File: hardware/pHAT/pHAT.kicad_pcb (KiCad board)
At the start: 2 copper layers, 65 x 30 mm, 5 parts, among them P1 Conn_02x20_Odd_Even

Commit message: First version of PCB for pHAT
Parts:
- added C0: 0.1µ, Capacitor_SMD:C_0805_2012Metric_Pad1.15x1.40mm_HandSolder, F.Cu at (224.1, 131.3)
- added C1: 4.7µ, Capacitor_SMD:C_0805_2012Metric_Pad1.15x1.40mm_HandSolder, F.Cu at (221.6, 131.3)
- added J_Air: Conn_01x04, Connector_Molex:Molex_KK-254_AE-6410-04A_1x04_P2.54mm_Vertical, F.Cu at (229.2, 146.8)
- added J_Hive: Conn_01x04, Connector_Molex:Molex_KK-254_AE-6410-04A_1x04_P2.54mm_Vertical, F.Cu at (241.3, 146.8)
- added J_Weight: Conn_01x02, Connector_Molex:Molex_KK-254_AE-6410-02A_1x02_P2.54mm_Vertical, F.Cu at (253.3, 146.8)
- added R0: 5K, Resistor_SMD:R_0805_2012Metric_Pad1.15x1.40mm_HandSolder, F.Cu at (218.4, 129.0)
- added R1: 5K, Resistor_SMD:R_0805_2012Metric_Pad1.15x1.40mm_HandSolder, F.Cu at (234.3, 131.3)
- added R2: 5K, Resistor_SMD:R_0805_2012Metric_Pad1.15x1.40mm_HandSolder, F.Cu at (231.8, 131.3)
- added R3: 5K, Resistor_SMD:R_0805_2012Metric_Pad1.15x1.40mm_HandSolder, F.Cu at (233.7, 138.5)
- added R4: 5K, Resistor_SMD:R_0805_2012Metric_Pad1.15x1.40mm_HandSolder, F.Cu at (237.5, 138.5)
- added R5: 5K, Resistor_SMD:R_0805_2012Metric_Pad1.15x1.40mm_HandSolder, F.Cu at (236.8, 131.3)
- added R6: 5K, Resistor_SMD:R_0805_2012Metric_Pad1.15x1.40mm_HandSolder, F.Cu at (239.4, 131.3)
- added R7: 5K, Resistor_SMD:R_0805_2012Metric_Pad1.15x1.40mm_HandSolder, F.Cu at (229.2, 131.3)
- added R8: 5K, Resistor_SMD:R_0805_2012Metric_Pad1.15x1.40mm_HandSolder, F.Cu at (226.7, 131.3)
- added U0: PCA9540B, Package_SO:TSSOP-8_3x3mm_P0.65mm, F.Cu at (235.6, 135.4)
- added U1: ADC101C021CIMK, Package_TO_SOT_SMD:SOT-23-6, F.Cu at (218.4, 131.6)
- moved MK1 26.0 mm to (203.5, 123.5)
- moved MK2 26.0 mm to (261.5, 123.5)
- moved MK3 26.0 mm to (203.5, 146.5)
- moved MK4 26.0 mm to (261.5, 146.5)
- moved P1 26.0 mm to (208.4, 124.8)
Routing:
- net +3V3: track 0.00 -> 132.2 mm
- net /AnalogIn: track 0.00 -> 54.0 mm
- net /SDA: track 0.00 -> 34.9 mm
- net /SCL: track 0.00 -> 33.2 mm
- net /SCL1: track 0.00 -> 25.7 mm
- net /SDA1: track 0.00 -> 24.9 mm
- net GND: track 0.00 -> 20.2 mm, vias 0 -> 1
- net /SCL0: track 0.00 -> 17.8 mm
- net /SDA0: track 0.00 -> 16.4 mm
- net Net-(R0-Pad1): track 0.00 -> 3.06 mm
- net Net-(R7-Pad2): track 0.00 -> 2.54 mm
- added copper zone on B.Cu, net GND
- added copper zone on F.Cu, net GND

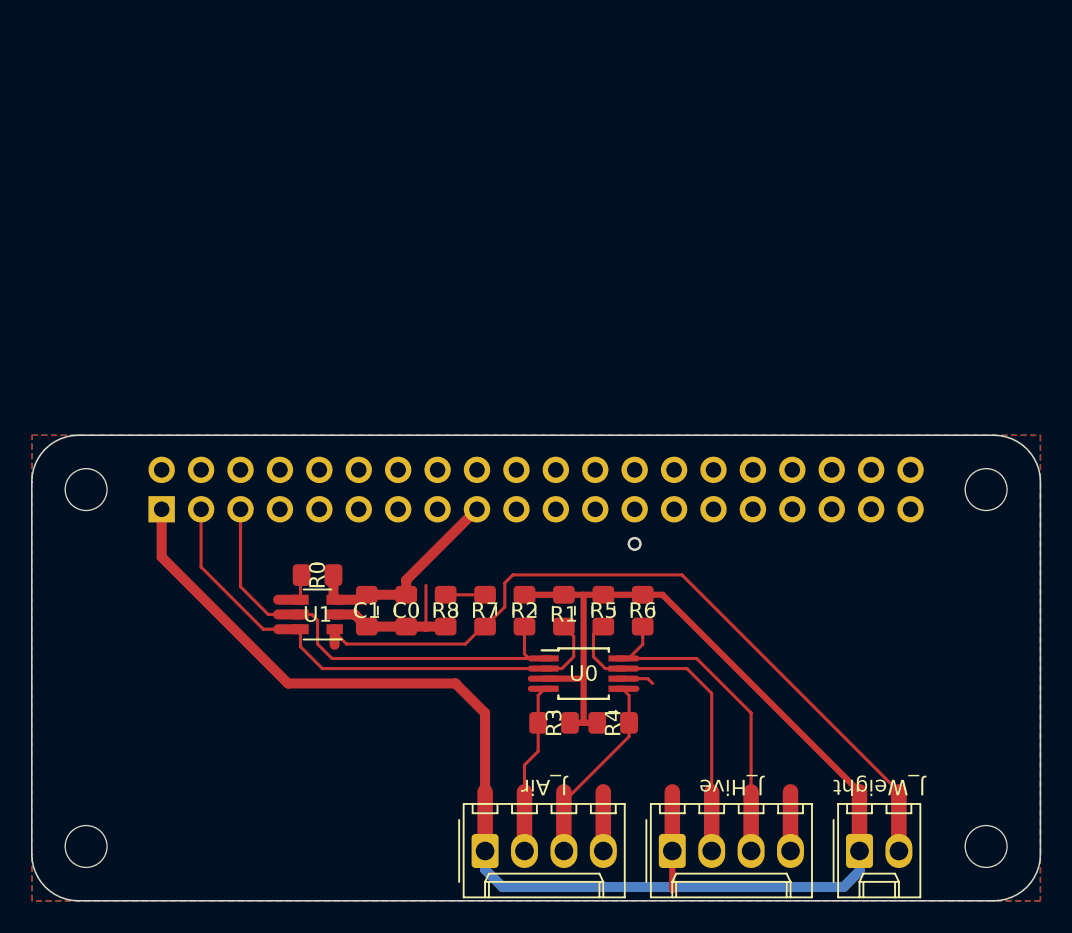
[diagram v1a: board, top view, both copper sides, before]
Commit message: graphical improvements to PCB
Added a logo and cleaned some tracks
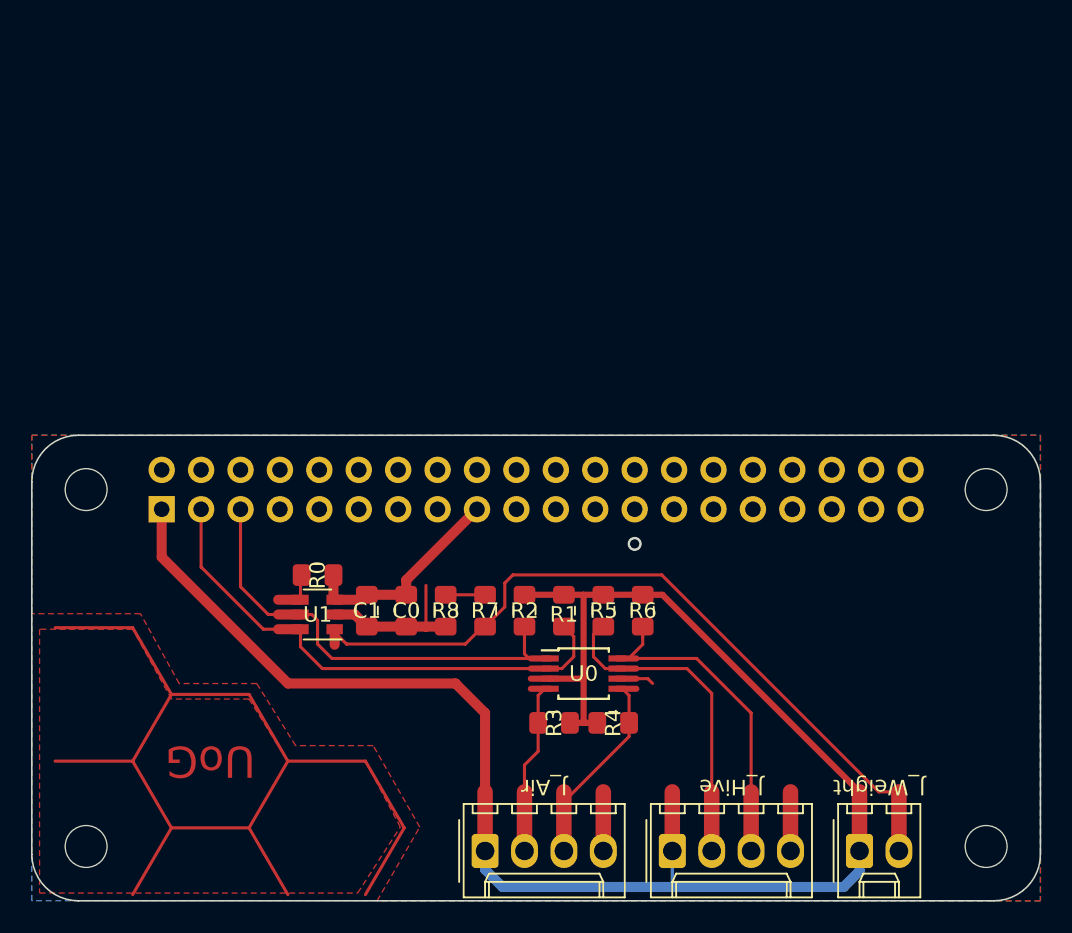
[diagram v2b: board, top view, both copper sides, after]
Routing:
- net Net-(P1-Pad10): track 0.00 -> 69.8 mm
- net +3V3: track 132.2 -> 129.7 mm
- added copper zone on F.Cu, net (none)
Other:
- rule trace_min: 0.1524 -> 0.2
- board text added: "UoG"

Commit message: First version of sensor board
Added a sensor board for the HIH61 humidity and temperature sensor
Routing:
- net Net-(P1-Pad10): track 69.8 -> 0.00 mm
- net +3V3: track 129.7 -> 199.4 mm

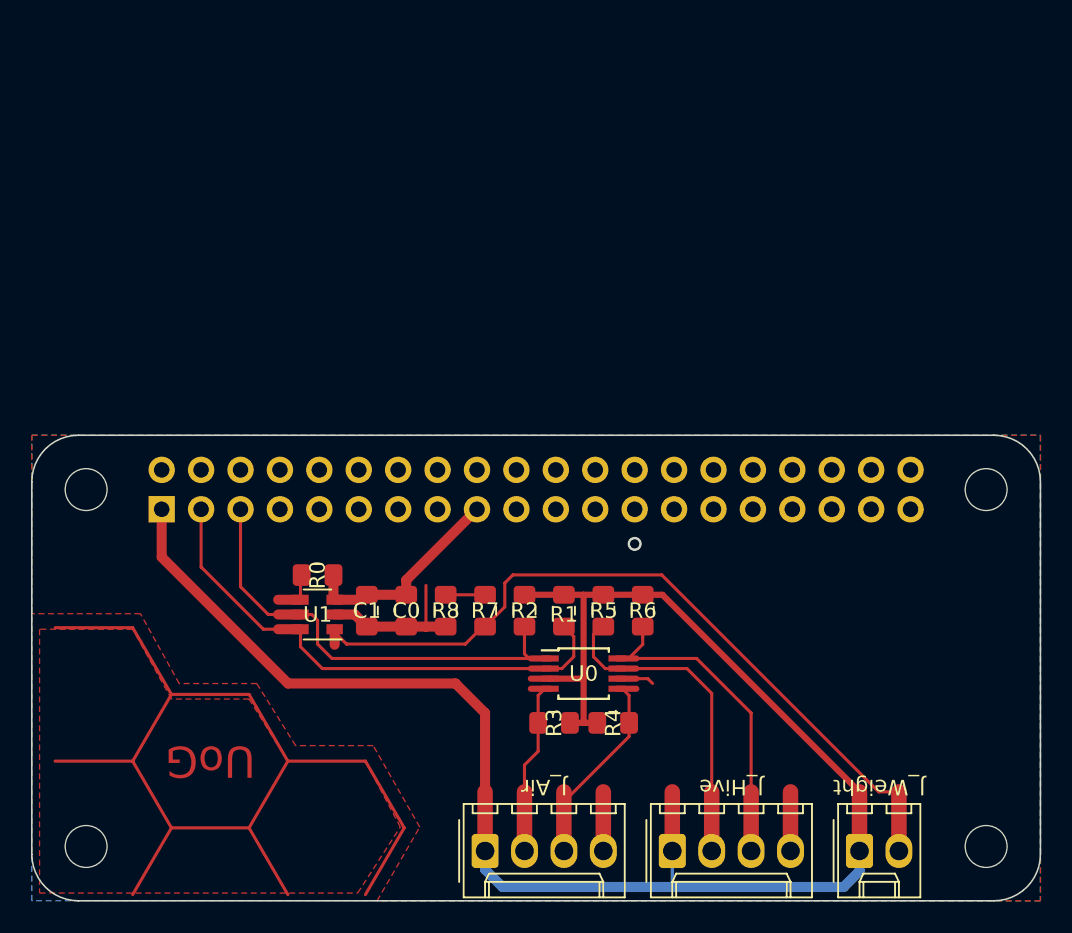
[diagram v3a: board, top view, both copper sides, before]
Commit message: Moving form multiplexer to two I2C busses
Changed from using one I2C bus with a multiplexer to using two I2C busses with the addition of level shifters
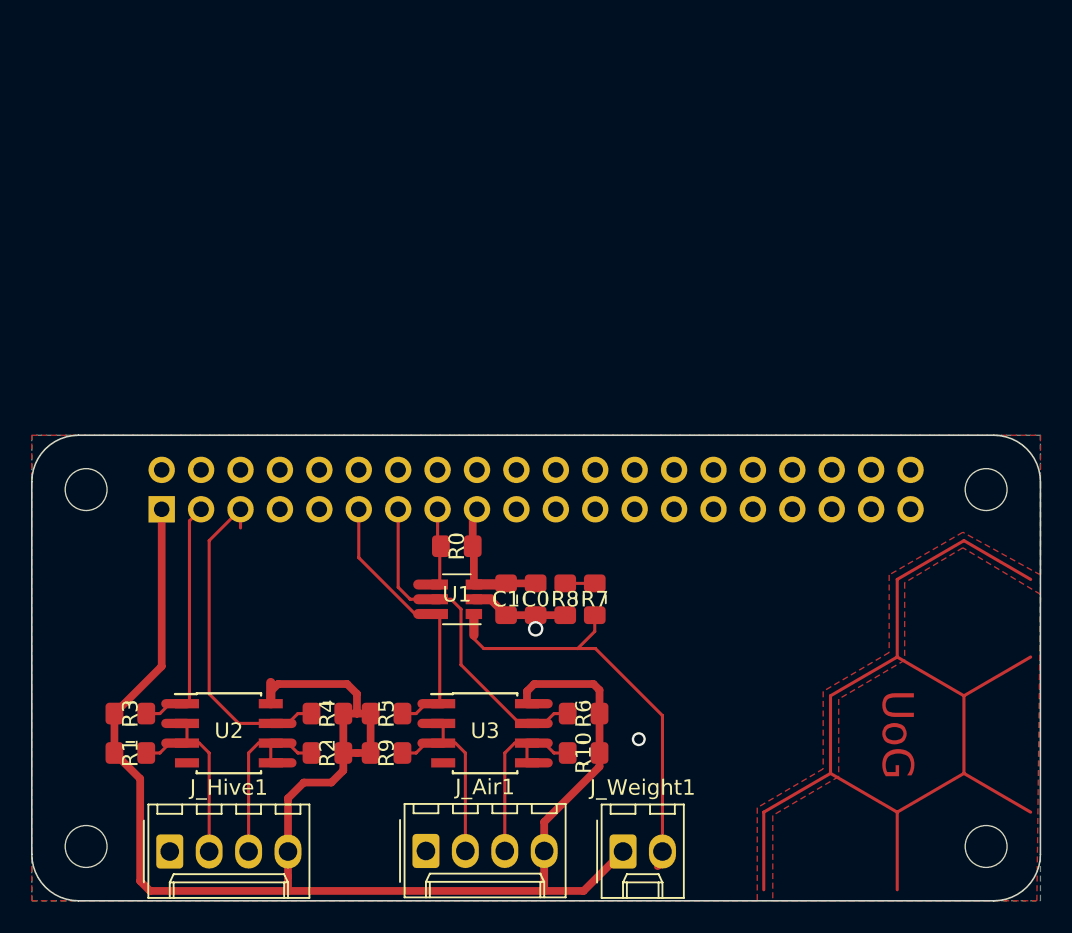
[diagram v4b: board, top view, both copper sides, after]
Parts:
- removed J_Air, J_Hive: Conn_01x04, Connector_Molex:Molex_KK-254_AE-6410-04A_1x04_P2.54mm_Vertical
- removed J_Weight: Conn_01x02, Connector_Molex:Molex_KK-254_AE-6410-02A_1x02_P2.54mm_Vertical
- removed U0: PCA9540B, Package_SO:TSSOP-8_3x3mm_P0.65mm
- added J_Air1: Conn_01x04, Connector_Molex:Molex_KK-254_AE-6410-04A_1x04_P2.54mm_Vertical, F.Cu at (225.4, 146.8)
- added J_Hive1: Conn_01x04, Connector_Molex:Molex_KK-254_AE-6410-04A_1x04_P2.54mm_Vertical, F.Cu at (208.9, 146.8)
- added J_Weight1: Conn_01x02, Connector_Molex:Molex_KK-254_AE-6410-02A_1x02_P2.54mm_Vertical, F.Cu at (238.1, 146.8)
- added R10: 5K, Resistor_SMD:R_0805_2012Metric_Pad1.15x1.40mm_HandSolder, F.Cu at (235.6, 140.5)
- added R9: 5K, Resistor_SMD:R_0805_2012Metric_Pad1.15x1.40mm_HandSolder, F.Cu at (222.9, 140.5)
- added U2: P82B96, Package_SO:SOIC-8_3.9x4.9mm_P1.27mm, F.Cu at (212.7, 139.2)
- added U3: P82B96, Package_SO:SOIC-8_3.9x4.9mm_P1.27mm, F.Cu at (229.2, 139.2)
- moved R1 29.4 mm to (206.3, 140.5), turned to 0 degrees
- moved R3 27.3 mm to (206.3, 137.9), turned to 0 degrees
- moved R4 18.4 mm to (219.1, 137.9), turned to 180 degrees
- moved R2 15.7 mm to (219.1, 140.5), turned to 180 degrees
- moved R5 15.5 mm to (222.9, 137.9), turned to 0 degrees
- moved R0 9.16 mm to (227.4, 127.1)
- moved U1 9.03 mm to (227.4, 130.6)
- moved C1 9.00 mm to (230.6, 130.6)
- moved C0 8.37 mm to (232.5, 130.6)
- moved R8 7.74 mm to (234.4, 130.6)
- moved R6 7.65 mm to (235.6, 137.9), turned to 180 degrees
- moved R7 7.11 mm to (236.3, 130.6)
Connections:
- P1 pad 11: Net-(P1-Pad11) -> /SDA1
- P1 pad 13: Net-(P1-Pad13) -> /SCL1
- P1 pad 15: Net-(P1-Pad15) -> /ADC_Alert
- P1 pad 3: /SDA -> /SDA0
- P1 pad 5: /SCL -> /SCL0
- R0 pad 1: Net-(R0-Pad1) -> /ADC_Alert
- R1 pad 2: /SDA -> /SDAH
- R2 pad 2: /SCL -> /SCLH
- U1 pad 4: Net-(R0-Pad1) -> /ADC_Alert
- U1 pad 5: /SCL -> /SCL1
- U1 pad 6: /SDA -> /SDA1
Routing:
- net /SDA: track 34.9 -> 0.00 mm
- net /SCL: track 33.2 -> 0.00 mm
- net /AnalogIn: track 54.0 -> 29.9 mm
- net /SDAH: track 0.00 -> 14.9 mm
- net /SCLH: track 0.00 -> 14.9 mm
- net /SDAA: track 0.00 -> 14.9 mm
- net /SCLA: track 0.00 -> 14.9 mm
- net GND: track 20.2 -> 8.30 mm, vias 1 -> 2
- net +3V3: track 199.4 -> 189.6 mm
- net /ADC_Alert: track 0.00 -> 6.36 mm
- net /SCL0: track 17.8 -> 22.9 mm
- net /SDA1: track 24.9 -> 19.8 mm
- net Net-(R0-Pad1): track 3.06 -> 0.00 mm
- net /SCL1: track 25.7 -> 23.3 mm
- net /SDA0: track 16.4 -> 17.2 mm
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
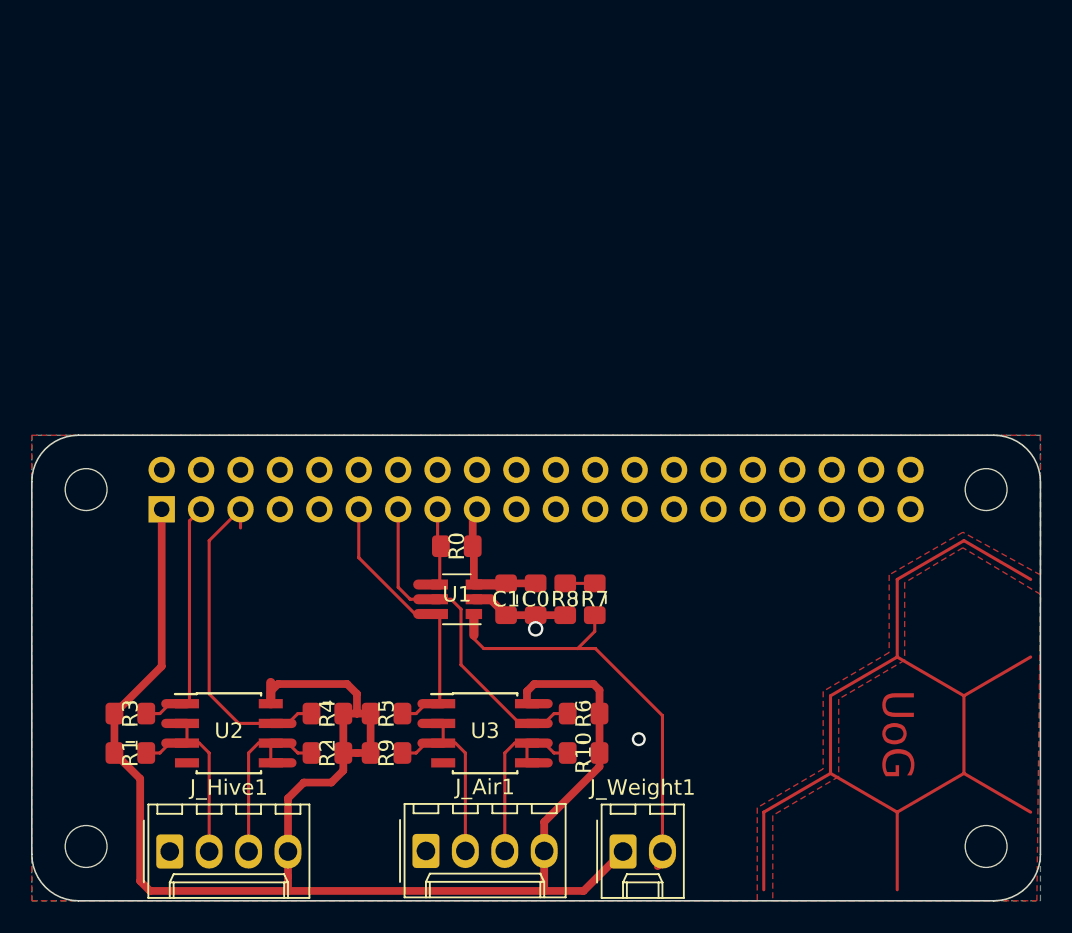
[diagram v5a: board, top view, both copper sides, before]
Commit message: Added the alarm pin for humidity
Added support for the alarm pin of the HIH6131 in order to detect through interrupt a high level of humidity
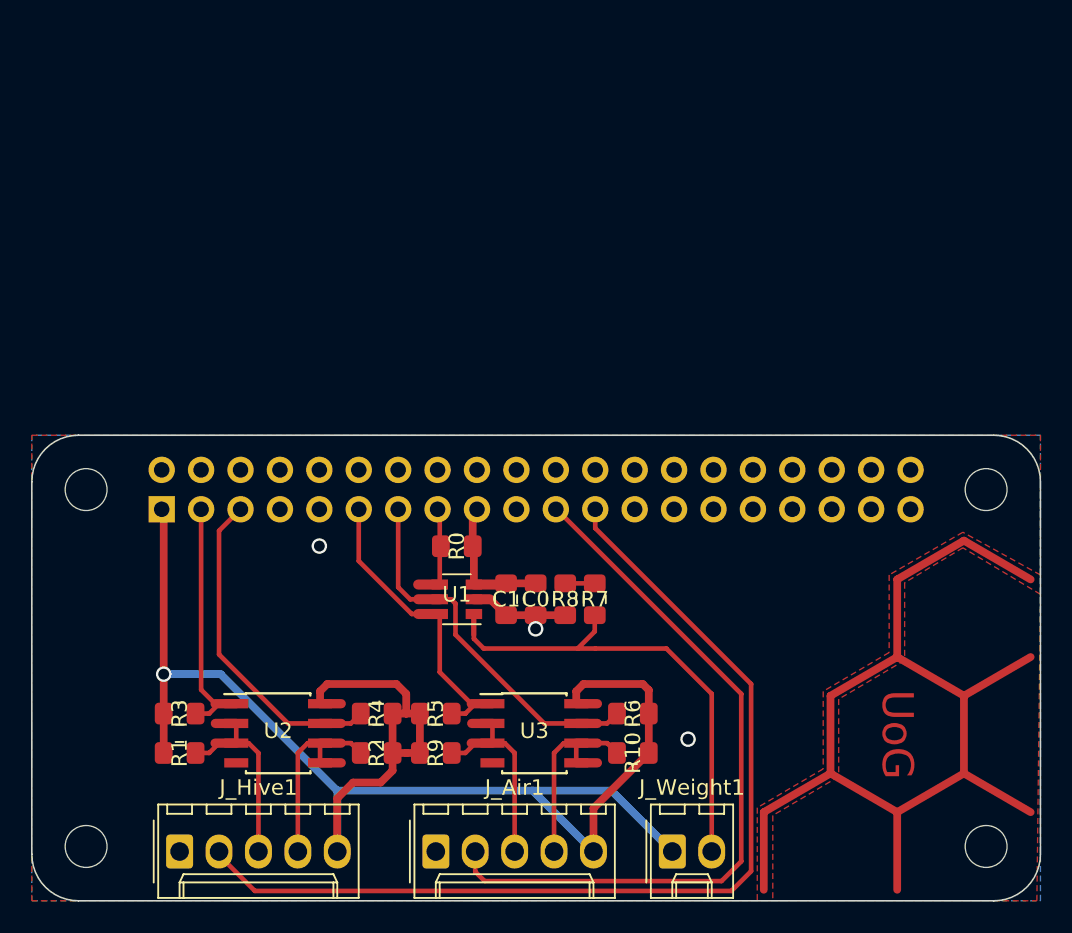
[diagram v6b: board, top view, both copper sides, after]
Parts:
- J_Air1, J_Hive1: value Conn_01x04 -> Conn_01x05; footprint Connector_Molex:Molex_KK-254_AE-6410-04A_1x04_P2.54mm_Vertical -> Connector_Molex:Molex_KK-254_AE-6410-05A_1x05_P2.54mm_Vertical
- moved J_Weight1 3.18 mm to (241.3, 146.8)
- moved R1 3.18 mm to (209.5, 140.5)
- moved R10 3.18 mm to (238.7, 140.5)
- moved R3 3.18 mm to (209.5, 137.9)
- moved R6 3.18 mm to (238.7, 137.9)
- moved U2 3.18 mm to (215.9, 139.2)
- moved R2 3.17 mm to (222.2, 140.5)
- moved R4 3.17 mm to (222.2, 137.9)
- moved R5 3.17 mm to (226.0, 137.9)
- moved R9 3.17 mm to (226.0, 140.5)
- moved U3 3.17 mm to (232.4, 139.2)
- moved J_Air1 0.64 mm to (226.0, 146.8)
- moved J_Hive1 0.64 mm to (209.5, 146.8)
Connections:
- J_Air1 pad 2: /SDAA -> /alarm_air
- J_Air1 pad 3: /SCLA -> /SDAA
- J_Air1 pad 4: +3V3 -> /SCLA
- J_Hive1 pad 2: /SDAH -> /alarm_hive
- J_Hive1 pad 3: /SCLH -> /SDAH
- J_Hive1 pad 4: +3V3 -> /SCLH
- P1 pad 21: Net-(P1-Pad21) -> /alarm_air
- P1 pad 23: Net-(P1-Pad23) -> /alarm_hive
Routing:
- net /alarm_hive: track 0.00 -> 63.5 mm
- net /alarm_air: track 0.00 -> 46.9 mm
- net /SCL1: track 23.3 -> 26.0 mm
- net /AnalogIn: track 29.9 -> 32.5 mm
- net +3V3: track 189.6 -> 187.1 mm, vias 0 -> 1
- net GND: track 8.30 -> 8.20 mm, vias 2 -> 3
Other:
- net class Default: clearance 0.2 -> 0.3; trace_width 0.2 -> 0.3
- net class Power: clearance 0.2 -> 0.3
- rule trace_clearance: 0.2 -> 0.3
